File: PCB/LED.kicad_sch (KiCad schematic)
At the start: 8 parts

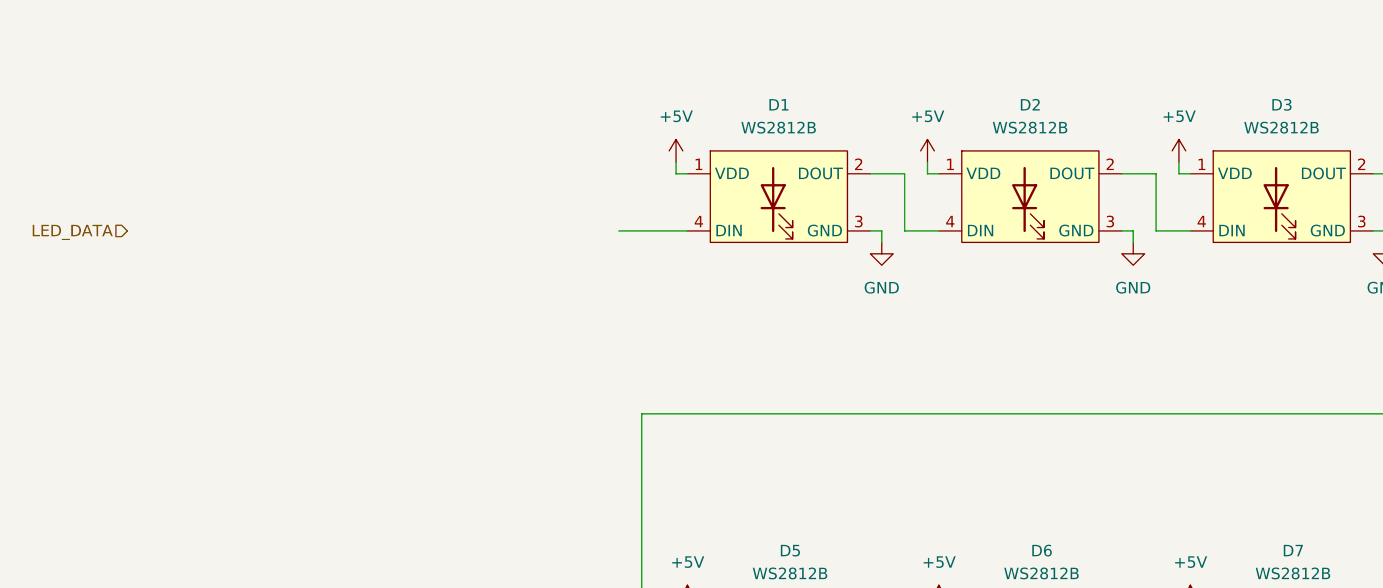
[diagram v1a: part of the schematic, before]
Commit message: Finish schematic minus mcu
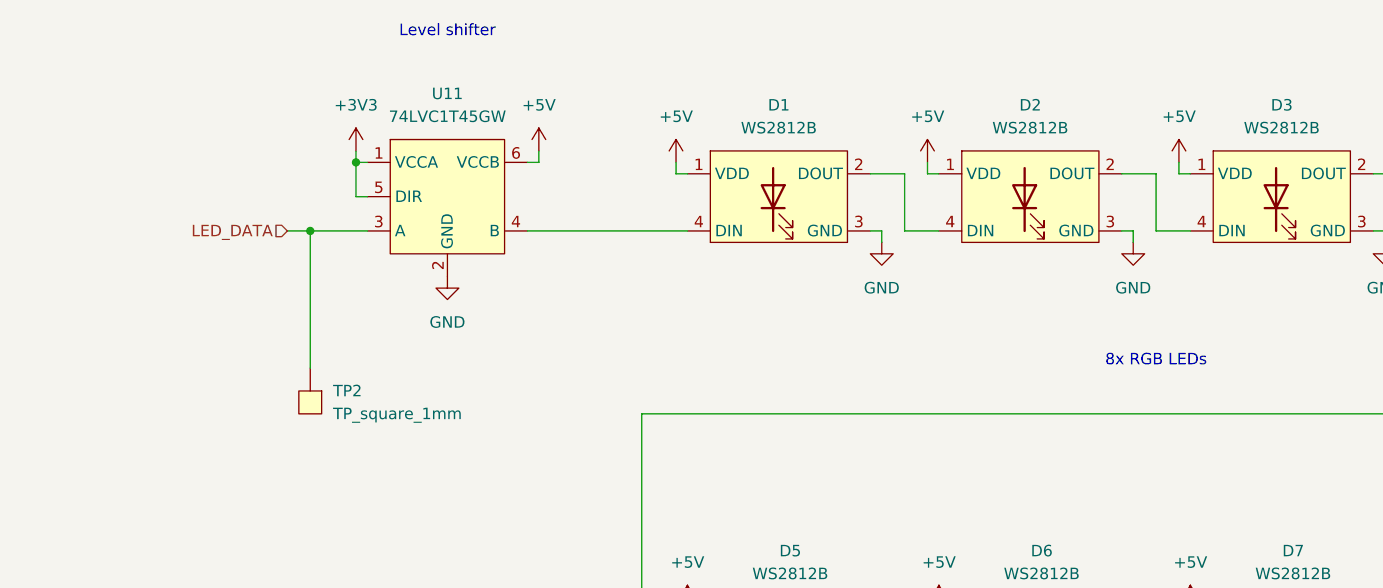
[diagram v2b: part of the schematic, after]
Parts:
- added TP2: TP_square_1mm, 011-Misc:Testpoint_square_1mm, symbol 011-Misc:Testpoint_square_1mm
- added U11: 74LVC1T45GW,125, 005-ICs:TSSOP6_SOT363-2.step, symbol 005-ICs:74LVC1T45GW,125
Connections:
- net +5V: now also U11.6 (VCCB)
- net GND: now also U11.2 (GND)
- net LED_DATA: now also TP2., U11.3 (A)
- net at D1.4 (DIN): now also U11.4 (B)
- new net +3V3: U11.1 (VCCA), U11.5 (DIR)
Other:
- note added: "8x RGB LEDs"
- note added: "Level shifter"

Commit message: WIP
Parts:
- added D10, D11, D9: COM-16347, 006-Diodes:COM-16347, symbol 006-Diodes:COM-16347
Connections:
- net +5V: now also D10.1 (VDD), D11.1 (VDD), D9.1 (VDD)
- net GND: now also D10.3 (GND), D11.3 (GND), D9.3 (GND)
- net at D8.2 (DOUT): now also D9.4 (DIN)
- new net: D10.2 (DOUT), D11.4 (DIN)
- new net: D10.4 (DIN), D9.2 (DOUT)
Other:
- note added: "3x RGB Information LEDs"
- note added: "8x RGB position LEDs"
- note removed: "8x RGB LEDs"

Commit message: Layout start
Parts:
- removed TP2: TP_square_1mm, 011-Misc:Testpoint_square_1mm, symbol 011-Misc:Testpoint_square_1mm
- removed U11: 74LVC1T45GW,125, 005-ICs:TSSOP6_SOT363-2.step, symbol 005-ICs:74LVC1T45GW,125
- added U7: 74LVC1T45GW.125, 005-ICs:TSSOP6_SOT363-2.step, symbol 005-ICs:74LVC1T45GW.125
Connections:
- net +3V3: now also U7.1 (VCCA), U7.5 (DIR)
- net +5V: now also U7.6 (VCCB)
- net GND: now also U7.2 (GND)
- net LED_DATA: now also U7.3 (A)
- net at D1.4 (DIN): now also U7.4 (B)

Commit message: First layout draft
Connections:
- net +3V3 renamed +3.3V
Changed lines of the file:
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@@
+	)
+	(symbol
+		(lib_id "power:+3.3V")
+		(at 54.61 40.64 0)
+		(unit 1)
+		(exclude_from_sim no)
+		(in_bom yes)
+		(on_board yes)
+		(dnp no)
+		(property "Reference" "#PWR054"
+			(at 54.61 44.45 0)
+			(effects
+				(font
+					(size 1.27 1.27)
+				)
+				(hide yes)
+			)
+		)
+		(property "Value" "+3.3V"
+			(at 54.864 36.322 0)
+			(effects
+				(font
+					(size 1.27 1.27)
+				)
+			)
+		)
+		(property "Footprint" ""
+			(at 54.61 40.64 0)
+			(effects
+				(font
+					(size 1.27 1.27)
+				)
+				(hide yes)
+			)
+		)
+		(property "Datasheet" ""
+			(at 54.61 40.64 0)
+			(effects
+				(font
+					(size 1.27 1.27)
+				)
+				(hide yes)
+			)
+		)
+		(property "Description" "Power symbol creates a global label with name \"+3.3V\""
+			(at 54.61 40.64 0)
+			(effects
+				(font
+					(size 1.27 1.27)
+				)
+				(hide yes)
+			)
+		)
+		(pin "1"
+		)
+		(instances
+			(project "relativeGPS"
+				(path "/9255e348-2f0c-48d3-8a71-46491dcb1a12/0163d1bd-977b-4b50-9d38-5cf06cb7c696"
+					(reference "#PWR054")
+					(unit 1)
+				)
+			)
+		)
 	)
 	(symbol
@@
 					(unit 1)
 				)
-			)
-		)
-	)
-	(symbol
-		(lib_id "power:+3V3")
-		(at 54.61 40.64 0)
-		(unit 1)
-		(exclude_from_sim no)
-		(in_bom yes)
-		(on_board yes)
-		(dnp no)
-		(fields_autoplaced yes)
-		(property "Reference" "#PWR054"
-			(at 54.61 44.45 0)
-			(effects
-				(font
-					(size 1.27 1.27)
-				)
-				(hide yes)
-			)
-		)
-		(property "Value" "+3V3"
-			(at 54.61 35.56 0)
-			(effects
-				(font
-					(size 1.27 1.27)
-				)
-			)
-		)
-		(property "Footprint" ""
-			(at 54.61 40.64 0)
-			(effects
-				(font
-					(size 1.27 1.27)
-				)
-				(hide yes)
-			)
-		)
-		(property "Datasheet" ""
-			(at 54.61 40.64 0)
-			(effects
-				(font
-					(size 1.27 1.27)
-				)
-				(hide yes)
-			)
-		)
-		(property "Description" "Power symbol creates a global label with name \"+3V3\""
-			(at 54.61 40.64 0)
-			(effects
-				(font
-					(size 1.27 1.27)
-				)
-				(hide yes)
-			)
-		)
-		(pin "1"
-		)
-		(instances
-			(project "relativeGPS"
-				(path "/9255e348-2f0c-48d3-8a71-46491dcb1a12/0163d1bd-977b-4b50-9d38-5cf06cb7c696"
-					(reference "#PWR054")
-					(unit 1)
-				)

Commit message: Add TPs
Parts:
- added TP14: TP_square_1mm, 011-Misc:Testpoint_square_1mm, symbol 011-Misc:Testpoint_square_1mm
- U7: footprint 005-ICs:TSSOP6_SOT363-2.step -> 005-ICs:TSSOP6_SOT363-2
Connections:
- net LED_DATA: now also TP14.1
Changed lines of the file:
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@@
 (kicad_sch
-	(version 20231120)
+	(version 20250114)
 	(generator "eeschema")
-	(generator_version "8.0")
+	(generator_version "9.0")
 	(paper "A4")
+	(text "3x RGB Information LEDs"
+		(exclude_from_sim no)
+		(at 141.732 116.586 0)
+		(effects
+			(font
+				(size 1.27 1.27)
+			)
+		)
+	)
+	(text "Level shifter"
+		(exclude_from_sim no)
+		(at 64.77 27.432 0)
+		(effects
+			(font
+				(size 1.27 1.27)
+			)
+		)
+	)
+	(text "8x RGB position LEDs"
+		(exclude_from_sim no)
+		(at 143.51 64.008 0)
+		(effects
+			(font
+				(size 1.27 1.27)
+			)
+		)
+	)
+	(junction
+		(at 50.8 49.53)
+		(diameter 0)
+		(color 0 0 0 0)
+	)
 	(junction
 		(at 54.61 41.91)
@@
 	(wire
 		(pts
+			(xy 50.8 49.53) (xy 50.8 54.61)
+		)
+		(stroke
+			(width 0)
+			(type default)
+		)
+	)
+	(wire
+		(pts
 			(xy 147.32 127) (xy 147.32 128.27)
 		)
@@
 	(wire
 		(pts
+			(xy 50.8 49.53) (xy 55.88 49.53)
+		)
+		(stroke
+			(width 0)
+			(type default)
+		)
+	)
+	(wire
+		(pts
 			(xy 142.24 135.89) (xy 142.24 134.62)
 		)
@@
 	(wire
 		(pts
-			(xy 46.99 49.53) (xy 55.88 49.53)
+			(xy 46.99 49.53) (xy 50.8 49.53)
 		)
 		(stroke
@@
 		)
 	)
-	(text "3x RGB Information LEDs"
-		(exclude_from_sim no)
-		(at 141.732 116.586 0)
-		(effects
-			(font
-				(size 1.27 1.27)
-			)
-		)
-	)
-	(text "Level shifter"
-		(exclude_from_sim no)
-		(at 64.77 27.432 0)
-		(effects
-			(font
-				(size 1.27 1.27)
-			)
-		)
-	)
-	(text "8x RGB position LEDs"
-		(exclude_from_sim no)
-		(at 143.51 64.008 0)
-		(effects
-			(font
-				(size 1.27 1.27)
-			)
-		)
-	)
 	(hierarchical_label "LED_DATA"
 		(shape input)
 		(at 46.99 49.53 180)
-		(fields_autoplaced yes)
 		(effects
 			(font
@@
 	)
 	(symbol
+		(lib_id "011-Misc:Testpoint_square_1mm")
+		(at 50.8 58.42 270)
+		(unit 1)
+		(exclude_from_sim no)
+		(in_bom no)
+		(on_board yes)
+		(dnp no)
+		(property "Reference" "TP14"
+			(at 52.578 58.42 90)
+			(effects
+				(font
+					(size 1.27 1.27)
+				)
+				(justify left)
+			)
+		)
+		(property "Value" "TP_square_1mm"
+			(at 43.942 60.96 90)
+			(effects
+				(font
+					(size 1.27 1.27)
+				)
+				(justify left)
+			)
+		)
+		(property "Footprint" "011-Misc:Testpoint_square_1mm"
+			(at 46.482 58.674 0)
+			(effects
+				(font
+					(size 1.27 1.27)
+				)
+				(hide yes)
+			)
+		)
+		(property "Datasheet" ""
+			(at 50.8 58.42 0)
+			(effects
+				(font
+					(size 1.27 1.27)
+				)
+				(hide yes)
+			)
+		)
+		(property "Description" ""
+			(at 50.8 58.42 0)
+			(effects
+				(font
+					(size 1.27 1.27)
+				)
+				(hide yes)
+			)
+		)
+		(pin "1"
+		)
+		(instances
+			(project ""
+				(path "/9255e348-2f0c-48d3-8a71-46491dcb1a12/0163d1bd-977b-4b50-9d38-5cf06cb7c696"
+					(reference "TP14")
+					(unit 1)
+				)
+			)
+		)
+	)
+	(symbol
 		(lib_id "power:GND")
 		(at 170.18 100.33 0)
@@
 			)
 		)
-		(property "Footprint" "005-ICs:TSSOP6_SOT363-2.step"
+		(property "Footprint" "005-ICs:TSSOP6_SOT363-2"
 			(at 65.024 78.994 0)
 			(effects
